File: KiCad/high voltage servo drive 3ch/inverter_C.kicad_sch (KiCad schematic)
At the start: 50 parts, among them U18 IPM

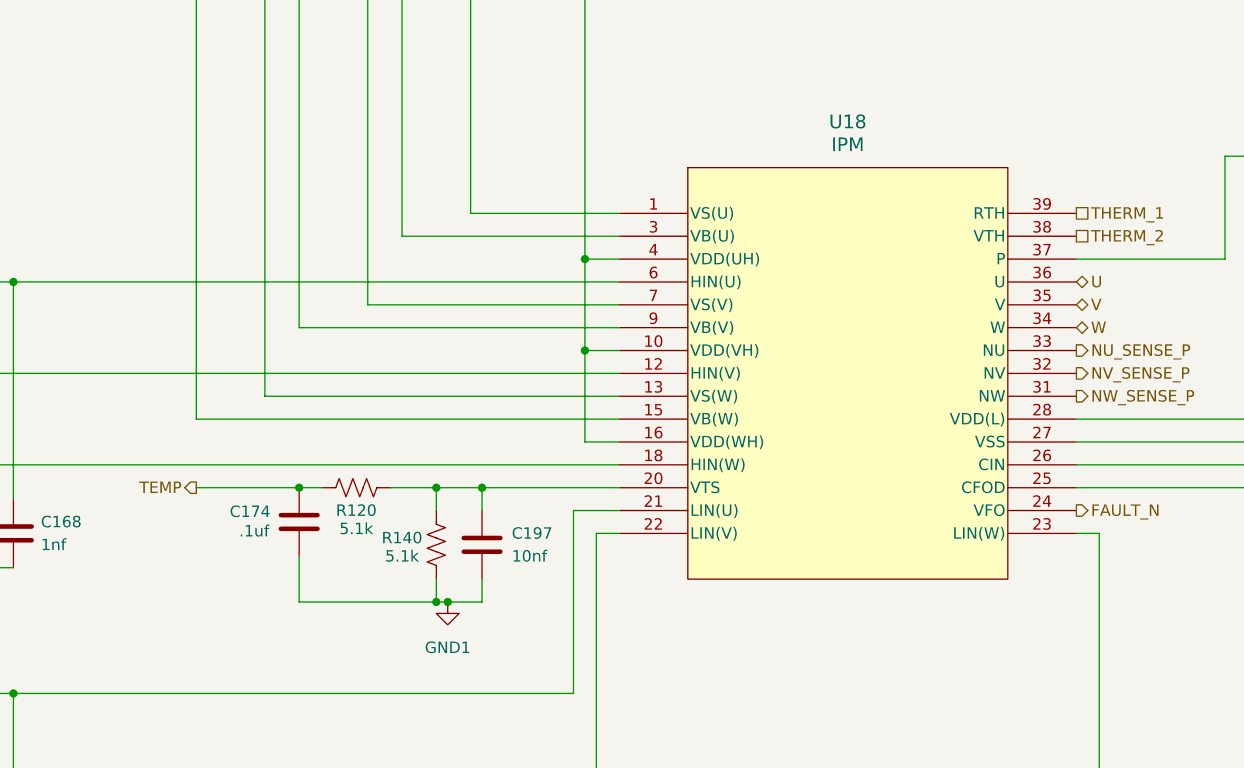
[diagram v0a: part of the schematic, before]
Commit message: add rev 0.2 changes and rev 0.1 mfg files
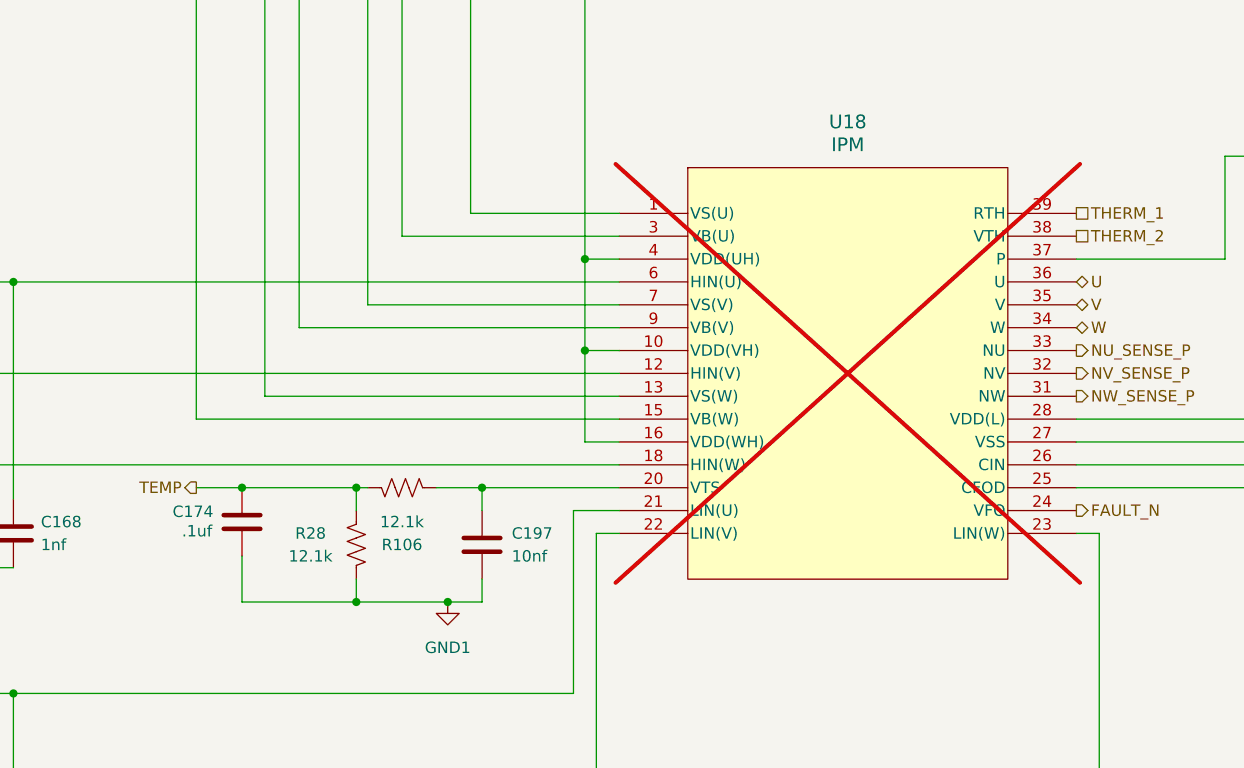
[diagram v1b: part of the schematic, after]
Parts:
- removed R120, R140: 5.1k, Resistor_SMD:R_0402_1005Metric, symbol Device:R_US
- added R106, R28: 12.1k, Resistor_SMD:R_0402_1005Metric, symbol Device:R_US
- U18: footprint DIP39_54.5X31.0_MODGC_OSI -> footprints:DIP39_54.5X31.0_MODGC_OSI; Generic Allowed? (none) -> no; now not fitted
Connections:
- net GND1: now also R28.2
- net TEMP: now also R106.1, R28.1
- net at C197.1, U18.20 (VTS): now also R106.2
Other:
- moved on the sheet: C174
